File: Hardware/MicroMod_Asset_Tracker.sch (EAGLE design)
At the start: 153 parts, among them J11 microSD, J17 NANO_SIM, J18 SARA_USB, J2 JTAG, J3 QWIIC_RIGHT_ANGLE, J4 MICROMOD-2222-C, J5 SPI, J6 SPI, J7 QWIIC_RIGHT_ANGLE, Q1 20V/0.2A/8MHz/1.2Ω/1Vth, Q10 20V/0.2A/8MHz/1.2Ω/1Vth, Q2 310mA/60V/1.6Ω, Q3 20V/0.2A/8MHz/1.2Ω/1Vth, Q4 310mA/60V/1.6Ω, Q5 20V/0.2A/8MHz/1.2Ω/1Vth, Q6 20V/4.2A/52mΩ/1.4W, Q7 20V/0.2A/8MHz/1.2Ω/1Vth, Q9 20V/0.2A/8MHz/1.2Ω/1Vth, U1 SARA-R5, U13 9DoF IMU, U14 1.8V/100mA, U2 MCP73831, U3 3.3V, U4 TXB0104, U5 AP7361C-33FGE, U6 TXB0104, U7 PCA9306, U8 74HC1G04

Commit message: Almost ready for airwire review
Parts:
- removed Q7, Q9: 20V/0.2A/8MHz/1.2Ω/1Vth, SparkFun-DiscreteSemi:MOSFET-NCH-RE1C00UNTL
- removed R40, R41, R44, R45, R46, R47: 2.2k, SparkFun-Resistors:2.2KOHM-0402T-1/16W-1%
- added D12: GREEN, SparkFun-LED:LED-GREEN0603
- added D13: BLUE, SparkFun-LED:LED-BLUE0603
- added JP6: JUMPER-SMT_2_NC_TRACE_SILK, SparkFun-Jumpers:JUMPER-SMT_2_NC_TRACE_SILK
- added R31, R36, R37: 0, SparkFun-Resistors:0OHM-0603-1/10W
- added R32, R33, R34, R35: 1k, SparkFun-Resistors:1KOHM-0603-1/10W-1%
- added U9: TXB0104, SparkFun-IC-Comms:TXB0104PWR
- C6: device SparkFun-Capacitors:4.7UF-0402_TIGHT-6.3V-20%-X5R -> SparkFun-Capacitors:4.7UF-0603-35V-(20%)
- Q1, Q3: value 20V/0.2A/8MHz/1.2Ω/1Vth -> 310mA/60V/1.6Ω; device SparkFun-DiscreteSemi:MOSFET-NCH-RE1C00UNTL -> SparkFun-DiscreteSemi:MOSFET-NCH-2N7002PW
- R14: device SparkFun-Resistors:2.2KOHM-0402T-1/16W-1% -> SparkFun-Resistors:2.2KOHM-0603-1/10W-1%
- R21: device SparkFun-Resistors:1KOHM-0402T-1/16W-1% -> SparkFun-Resistors:1KOHM-0603-1/10W-1%
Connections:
- new net N$29: JP6.1, R22.2
- new net N$31: R31.2, U1.V_INT
- new net N$32: Q1.G, R32.2
- new net N$33: Q1.D, R33.1
- new net N$34: D12.C, R33.2
- new net N$35: Q3.G, R34.2
- new net N$36: Q3.D, R35.1
- new net N$37: D13.C, R35.2
- new net N$38: R36.2, U1.RXD_O
- new net N$39: R37.2, U1.TXD_I
- new net SARA_NI: R34.1, U1.GPIO1
- new net SARA_TP: R32.1, U1.GPIO6/TP
- net 1.8V: now also U9.OE, U9.VCCA
- net 3.3V: now also D12.A, D13.A, JP6.2, U9.VCCB; no longer R22.2, R45.2, R47.2
- net GND: now also Q1.S, Q3.S, U9.GND
- net ICM-20948-LV_!CS!: now also U9.A4; no longer Q9.S, R46.1
- net ICM-20948-LV_#_1.8V: no longer Q1.G, Q3.G, Q7.G, Q9.G, R40.2, R41.2, R44.2, R46.2
- net ICM-20948-LV_INT: now also U9.A1; no longer Q7.S, R44.1
- net ICM-20948-LV_SCK: now also U9.A3; no longer Q1.S, R40.1
- net ICM-20948-LV_SDI: now also U9.A2; no longer Q3.S, R41.1
- net ICM_!CS!: now also U9.B4; no longer Q9.D, R47.1
- net ICM_INT: now also U9.B1; no longer Q7.D, R45.1
- net SARA_RXD: now also R36.1; no longer U1.RXD_O
- net SARA_TXD: now also R37.1; no longer U1.TXD_I
- net SPI_SCK: now also U9.B3; no longer Q1.D
- net SPI_SDO: now also U9.B2; no longer Q3.D
- net VCCIO: now also R31.1; no longer U1.V_INT
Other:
- note added: "IMU Voltage Regulator"
- note added: "SARA LEDs"
- note removed: "Controller Out Peripheral In (COPI)"
- note removed: "Voltage Regulator"
- moved on the sheet: C52, C53, C54, Q10, R22, R48, U14

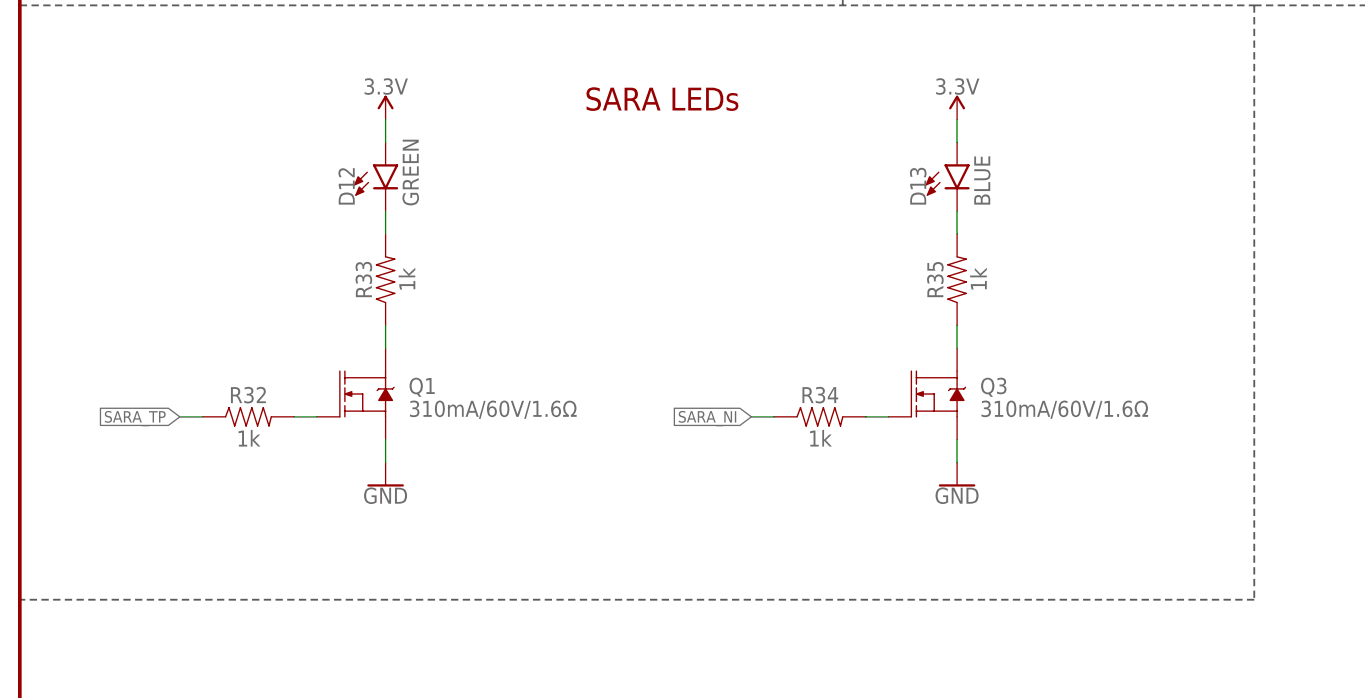
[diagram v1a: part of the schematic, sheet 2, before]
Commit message: Ready for airwire review
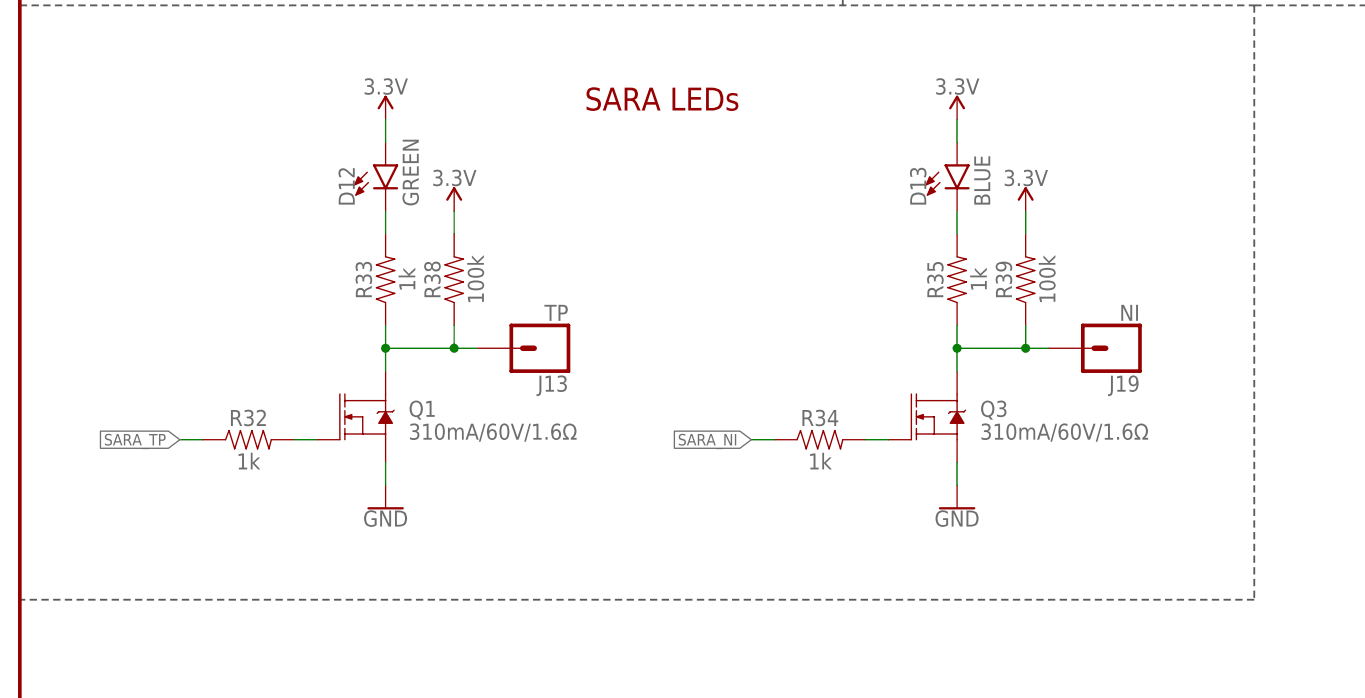
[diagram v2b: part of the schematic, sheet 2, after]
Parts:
- added J13: TP, SparkFun-Connectors:CONN_01PTH_NO_SILK_YES_STOP
- added J19: NI, SparkFun-Connectors:CONN_01PTH_NO_SILK_YES_STOP
- added R38, R39: 100k, SparkFun-Resistors:100KOHM-0603-1/10W-1%
- C51, C52: device SparkFun-Capacitors:0.1UF-0402T-16V-10% -> SparkFun-Capacitors:0.1UF-0603-25V-5%
- C53, C54: device SparkFun-Capacitors:1.0UF-0402T-16V-10% -> SparkFun-Capacitors:1.0UF-0603-16V-10%-X7R
- FB1: value FERRITE_BEAD-120_OHM-0402 -> 30Ω/1.8A; device SparkFun-Coils:FERRITE_BEAD-120_OHM-0402 -> SparkFun-Coils:FERRITE_BEAD-0603
- J9: value (none) -> !RST!
- R22, R29, R30, R48: device SparkFun-Resistors:2.2KOHM-0402T-1/16W-1% -> SparkFun-Resistors:2.2KOHM-0603-1/10W-1%
- R23: device SparkFun-Resistors:10KOHM-0402T-1/16W-1% -> SparkFun-Resistors:10KOHM-0603-1/10W-1%
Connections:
- removed net ICM-20948-LV_#_1.8V: C52.1, C53.1, Q10.G, R48.2, U13.VDD, U13.VDDIO, U14.OUT
- net 1.8V: now also C52.1, C53.1, Q10.G, R48.2, U13.VDD, U13.VDDIO, U14.OUT
- net 3.3V: now also R38.2, R39.2
- net N$33: now also J13.1, R38.1
- net N$36: now also J19.1, R39.1
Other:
- moved on the sheet: JP6, Q1, Q3, R32, R34

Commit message: Updates to support the ESP32 PB
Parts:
- removed E2: ICS-43434, Teensy:ICS-43434
- removed EN1: JUMPER-SMT_2_NC_TRACE_SILK, SparkFun-Jumpers:JUMPER-SMT_2_NC_TRACE_SILK
- removed EN2: JUMPER-SMT_2_NO_SILK, SparkFun-Jumpers:JUMPER-SMT_2_NO_SILK
- removed J3: QWIIC_RIGHT_ANGLE, SparkFun-Connectors:QWIIC_CONNECTORJS-1MM
- removed S4: BOOT, SparkFun-Switches:MOMENTARY-SWITCH-SPST-SMD-5.2-TALL-REDUNDANT
- added D14: WHITE, SparkFun-LED:LED-WHITE0603
- added EN, JP10, JP11, JP12, JP13, JP14, JP15, JP16, JP17, JP18, JP19, JP20: JUMPER-SMT_2_NC_TRACE_SILK, SparkFun-Jumpers:JUMPER-SMT_2_NC_TRACE_SILK
- added JP21, JP7, JP8, JP9: JUMPER-SMT_2_NO_SILK, SparkFun-Jumpers:JUMPER-SMT_2_NO_SILK
- added Q7: 310mA/60V/1.6Ω, SparkFun-DiscreteSemi:MOSFET-NCH-2N7002PW
- added R40, R41, R44: 100k, SparkFun-Resistors:100KOHM-0603-1/10W-1%
- added R42, R43: 1k, SparkFun-Resistors:1KOHM-0603-1/10W-1%
- added TP1, TP10, TP11, TP12, TP14, TP15, TP16, TP17, TP18, TP19, TP2, TP20, TP21, TP3, TP4, TP5, TP6, TP7, TP8, TP9: TEST-POINT3, SparkFun-Connectors:TEST-POINT3
- D9: value RGB -> 3.3V; device SparkFun-LED:LED-RGBPLCC-6 -> SparkFun-DiscreteSemi:DIODE-ZENER-MM3Z3V3T1G
- R16, R17, R18: value 1k -> 100k; device SparkFun-Resistors:1KOHM-0603-1/10W-1% -> SparkFun-Resistors:100KOHM-0603-1/10W-1%
- R25: value 10k -> 100k; device SparkFun-Resistors:10KOHM-0603-1/10W-1% -> SparkFun-Resistors:100KOHM-0603-1/10W-1%
- R33: value 1k -> 470; device SparkFun-Resistors:1KOHM-0603-1/10W-1% -> SparkFun-Resistors:470OHM-0603-1/10W-1%
- S1: value SWITCH1 -> RESET
- S2: value SWITCH2 -> BOOT
- S3: value RESET -> SARA_PWR
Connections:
- removed net BLUE: J4.G2/BUS2, R18.1
- removed net GREEN: J4.G1/BUS1, R17.1, R20.1, S1.2
- removed net I2C_!INT!: J4.I2C_!INT!, Q5.D, R30.1
- removed net I2C_SCL1: J14.4, J3.4, J4.I2C_SCL1, R4.1, U7.SCL2
- removed net I2C_SDA1: J14.3, J3.3, J4.I2C_SDA1, R1.1, U7.SDA2
- removed net I2S_SD: E2.SD, J4.AUD_IN/CAM_PCLK
- removed net RED: J4.G0/BUS0, R16.1
- removed net SARA_DCD: U1.DCD_O, U6.A2
- removed net SARA_DSR: U1.DSR_O, U6.A4
- removed net SARA_DTR: U1.DTR_I, U6.A1
- removed net SARA_EXT_INT: Q5.S, R29.1, U1.EXT_INT
- removed net SARA_RI: U1.RI_O, U6.A3
- removed net SPI_!CS!: J11.DAT3/!CS!, J4.SPI_!CS!
- removed net SWITCH2: J4.G3/BUS3, R19.1, S2.2
- new net N$40: J4.G1/BUS1, JP11.1
- new net N$41: J4.G2/BUS2, JP12.1
- new net N$42: J4.G3/BUS3, JP13.1
- new net N$43: J4.G4/BUS4, JP14.1
- new net N$44: J4.G5/BUS5, JP15.1
- new net N$45: J4.G6/BUS6, JP16.1
- new net N$46: J4.G7/BUS7, JP17.1
- new net N$47: Q7.G, R42.2
- new net N$48: J4.G10/ADC_D+/CAM_VSYNC, JP19.1
- new net N$49: D14.C, R43.2
- new net N$50: J4.G9/ADC_D-/CAM_HSYNC, JP21.1
- new net N$51: J4.AUD_LRCLK, JP20.1
- new net N$52: J4.AUD_BCLK, JP18.1
- new net SARA_DCD/RXD2O: TP15.1, U1.DCD_O, U6.A2
- new net SARA_DSR/RTS2I: TP17.1, U1.DSR_O, U6.A4
- new net SARA_DTR/TXD2I: TP14.1, U1.DTR_I, U6.A1
- new net SARA_INT: JP15.2, Q5.D, R30.1, TP12.1
- new net SARA_INT_1.8V: Q5.S, R29.1, TP11.1, U1.EXT_INT
- new net SARA_ON: JP19.2, JP21.2, Q7.D, R43.1, R44.1
- new net SARA_RI/CTS2O: TP16.1, U1.RI_O, U6.A3
- new net SARA_SCL_1.8V: TP10.1, U1.SCL, U7.SCL1
- new net SARA_SDA_1.8V: TP9.1, U1.SDA, U7.SDA1
- new net SD_!CS!: J11.DAT3/!CS!, JP10.2, R41.1
- net !BOOT!: now also S2.2; no longer S4.2
- net !RESET!: now also S1.2; no longer S3.2
- net 3.3V: now also D14.A, EN.2, R16.2, R41.2, R44.2; no longer D9.BLU-A, D9.GRN-A, D9.RED-A, EN1.2, EN2.2, J3.2, R19.2, R20.2
- net ANT_GNSS_PWR_EN: now also D9.C, JP16.2; no longer J4.G5/BUS5
- net CTS1: now also TP7.1
- net DCD: now also J4.RX2, TP19.1; no longer J4.SDIO_DATA2
- net DSR: now also JP17.2, R20.2, TP21.1; no longer J4.SPI_SDI1/SDIO_DATA0
- net DTR: now also J4.TX2, R40.1, TP18.1; no longer J4.SPI_!CS1!/SDIO_DATA3
- net GND: now also D9.A, JP9.1, Q7.S, R17.1, R18.2, R19.1, R40.2, S3.2; no longer E2.!L!R, E2.GND, J3.1, R25.1, S3.1, S4.1
- net I2S_SCK/PDM_CLK: now also JP18.2; no longer E2.SCK, J4.AUD_BCLK
- net I2S_WS/PDM_DAT: now also JP20.2; no longer E2.WS, J4.AUD_LRCLK
- net ICM_!CS!: now also J4.SPI_!CS!; no longer J4.G6/BUS6
- net ICM_INT: now also J4.I2C_!INT!; no longer J4.G7/BUS7
- net ICM_PWR: now also JP13.2, R16.1; no longer J4.SPI_SDO1/SDIO_CMD
- net LTE_PWR_ON: now also JP12.2, R18.1; no longer J4.G4/BUS4
- net MICROSD_PWR: now also JP11.2, R17.2; no longer J4.SPI_SCK1/SDIO_CLK
- net N$17: now also J4.I2C_SDA1, JP8.2; no longer D9.GRN-C, R17.2
- net N$18: now also JP9.2, R20.1; no longer D9.BLU-C, R18.2
- net N$19: now also J4.G0/BUS0, JP10.1; no longer D9.RED-C, R16.2
- net N$4: now also EN.1; no longer EN1.1
- net N$5: now also J4.I2C_SCL1, JP7.2; no longer E2.VDD, EN2.1
- net RI: now also JP14.2, TP20.1; no longer J4.SDIO_DATA1
- net RTS1: now also R19.2, TP8.1
- net RX1: now also TP5.1
- net SARA_CTS: now also TP3.1
- net SARA_PWR_ON: now also S3.1
- net SARA_RTS: now also TP4.1
- net SARA_RXD: now also TP1.1
- net SARA_SCL: now also J14.4, JP7.1, R4.1, U7.SCL2; no longer U1.SCL, U7.SCL1
- net SARA_SDA: now also J14.3, JP8.1, R1.1, U7.SDA2; no longer U1.SDA, U7.SDA1
- net SARA_TXD: now also TP2.1
- net TX1: now also TP6.1
- net VCCIO: now also R42.1
- net VIN: now also R25.1
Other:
- note added: "SARA I2C (3.3V)"
- note removed: "RGB LED"
- moved on the sheet: C17, C20, C21, C22, C23, C31, C46, C51, C52, C53, C54, D11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

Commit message: Work in progress - 14 airwires left!
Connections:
- net N$23 renamed VREG_3.3V
- net SIM_CLK: now also D8.1; no longer D8.6
- net SIM_IO: now also D8.6; no longer D8.4
- net SIM_RST: now also D8.4; no longer D8.3
- net VSIM: now also D8.3; no longer D8.1
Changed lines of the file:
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@@
 <segment>
 <pinref part="J17" gate="G$1" pin="VCC"/>
-<wire x1="309.88" y1="147.32" x2="279.4" y2="147.32" width="0.1524" layer="91"/>
-<wire x1="279.4" y1="147.32" x2="271.78" y2="147.32" width="0.1524" layer="91"/>
+<wire x1="309.88" y1="147.32" x2="281.94" y2="147.32" width="0.1524" layer="91"/>
 <label x="259.08" y="147.32" size="1.27" layer="95" rot="R180" xref="yes"/>
-<pinref part="D8" gate="G$1" pin="1"/>
+<wire x1="281.94" y1="147.32" x2="271.78" y2="147.32" width="0.1524" layer="91"/>
 <wire x1="271.78" y1="147.32" x2="261.62" y2="147.32" width="0.1524" layer="91"/>
 <wire x1="261.62" y1="147.32" x2="259.08" y2="147.32" width="0.1524" layer="91"/>
-<wire x1="284.48" y1="132.08" x2="279.4" y2="132.08" width="0.1524" layer="91"/>
-<wire x1="279.4" y1="132.08" x2="279.4" y2="147.32" width="0.1524" layer="91"/>
-<junction x="279.4" y="147.32"/>
 <pinref part="C12" gate="G$1" pin="2"/>
 <wire x1="261.62" y1="149.86" x2="261.62" y2="147.32" width="0.1524" layer="91"/>
@@
 <wire x1="271.78" y1="149.86" x2="271.78" y2="147.32" width="0.1524" layer="91"/>
 <junction x="271.78" y="147.32"/>
+<pinref part="D8" gate="G$1" pin="3"/>
+<wire x1="284.48" y1="127" x2="281.94" y2="127" width="0.1524" layer="91"/>
+<wire x1="281.94" y1="127" x2="281.94" y2="147.32" width="0.1524" layer="91"/>
+<junction x="281.94" y="147.32"/>
 </segment>
 <segment>
@@
 <segment>
 <pinref part="J17" gate="G$1" pin="IO"/>
-<wire x1="309.88" y1="144.78" x2="299.72" y2="144.78" width="0.1524" layer="91"/>
-<wire x1="299.72" y1="144.78" x2="284.48" y2="144.78" width="0.1524" layer="91"/>
+<wire x1="309.88" y1="144.78" x2="302.26" y2="144.78" width="0.1524" layer="91"/>
 <label x="259.08" y="144.78" size="1.27" layer="95" rot="R180" xref="yes"/>
-<pinref part="D8" gate="G$1" pin="4"/>
+<wire x1="302.26" y1="144.78" x2="284.48" y2="144.78" width="0.1524" layer="91"/>
 <wire x1="284.48" y1="144.78" x2="259.08" y2="144.78" width="0.1524" layer="91"/>
-<wire x1="297.18" y1="127" x2="299.72" y2="127" width="0.1524" layer="91"/>
-<wire x1="299.72" y1="127" x2="299.72" y2="144.78" width="0.1524" layer="91"/>
-<junction x="299.72" y="144.78"/>
 <pinref part="C10" gate="G$1" pin="2"/>
 <wire x1="284.48" y1="149.86" x2="284.48" y2="144.78" width="0.1524" layer="91"/>
 <junction x="284.48" y="144.78"/>
+<pinref part="D8" gate="G$1" pin="6"/>
+<wire x1="297.18" y1="132.08" x2="302.26" y2="132.08" width="0.1524" layer="91"/>
+<wire x1="302.26" y1="132.08" x2="302.26" y2="144.78" width="0.1524" layer="91"/>
+<junction x="302.26" y="144.78"/>
 </segment>
 <segment>
@@
 <segment>
 <pinref part="J17" gate="G$1" pin="CLK"/>
-<wire x1="309.88" y1="142.24" x2="302.26" y2="142.24" width="0.1524" layer="91"/>
-<wire x1="302.26" y1="142.24" x2="271.78" y2="142.24" width="0.1524" layer="91"/>
+<wire x1="309.88" y1="142.24" x2="279.4" y2="142.24" width="0.1524" layer="91"/>
 <label x="259.08" y="142.24" size="1.27" layer="95" rot="R180" xref="yes"/>
-<pinref part="D8" gate="G$1" pin="6"/>
+<wire x1="279.4" y1="142.24" x2="271.78" y2="142.24" width="0.1524" layer="91"/>
 <wire x1="271.78" y1="142.24" x2="259.08" y2="142.24" width="0.1524" layer="91"/>
-<wire x1="297.18" y1="132.08" x2="302.26" y2="132.08" width="0.1524" layer="91"/>
-<wire x1="302.26" y1="132.08" x2="302.26" y2="142.24" width="0.1524" layer="91"/>
-<junction x="302.26" y="142.24"/>
 <pinref part="C8" gate="G$1" pin="1"/>
 <wire x1="271.78" y1="134.62" x2="271.78" y2="142.24" width="0.1524" layer="91"/>
 <junction x="271.78" y="142.24"/>
+<pinref part="D8" gate="G$1" pin="1"/>
+<wire x1="284.48" y1="132.08" x2="279.4" y2="132.08" width="0.1524" layer="91"/>
+<wire x1="279.4" y1="132.08" x2="279.4" y2="142.24" width="0.1524" layer="91"/>
+<junction x="279.4" y="142.24"/>
 </segment>
 <segment>
@@
 <segment>
 <pinref part="J17" gate="G$1" pin="RST"/>
-<wire x1="309.88" y1="139.7" x2="281.94" y2="139.7" width="0.1524" layer="91"/>
-<wire x1="281.94" y1="139.7" x2="261.62" y2="139.7" width="0.1524" layer="91"/>
+<wire x1="309.88" y1="139.7" x2="299.72" y2="139.7" width="0.1524" layer="91"/>
 <label x="259.08" y="139.7" size="1.27" layer="95" rot="R180" xref="yes"/>
-<pinref part="D8" gate="G$1" pin="3"/>
+<wire x1="299.72" y1="139.7" x2="261.62" y2="139.7" width="0.1524" layer="91"/>
 <wire x1="261.62" y1="139.7" x2="259.08" y2="139.7" width="0.1524" layer="91"/>
-<wire x1="284.48" y1="127" x2="281.94" y2="127" width="0.1524" layer="91"/>
-<wire x1="281.94" y1="127" x2="281.94" y2="139.7" width="0.1524" layer="91"/>
-<junction x="281.94" y="139.7"/>
 <pinref part="C7" gate="G$1" pin="1"/>
 <wire x1="261.62" y1="134.62" x2="261.62" y2="139.7" width="0.1524" layer="91"/>
 <junction x="261.62" y="139.7"/>
+<pinref part="D8" gate="G$1" pin="4"/>
+<wire x1="297.18" y1="127" x2="299.72" y2="127" width="0.1524" layer="91"/>
+<wire x1="299.72" y1="127" x2="299.72" y2="139.7" width="0.1524" layer="91"/>
+<junction x="299.72" y="139.7"/>
 </segment>
 <segment>
@@
 </segment>
 </net>
-<net name="N$23" class="0">
+<net name="VREG_3.3V" class="0">
 <segment>
 <pinref part="C4" gate="G$1" pin="1"/>
@@
 <wire x1="144.78" y1="259.08" x2="142.24" y2="259.08" width="0.1524" layer="91"/>
 <junction x="142.24" y="259.08"/>
+<label x="127" y="259.08" size="1.27" layer="95"/>
 </segment>
 </net>
